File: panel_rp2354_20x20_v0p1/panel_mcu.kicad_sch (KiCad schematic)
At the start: 32 parts, among them SW1 SW_Push, SW2 SW_Push, U1 APS6404L-3SQR, U2 RP2354B_80QFN, Y1 ABM8-272-T3

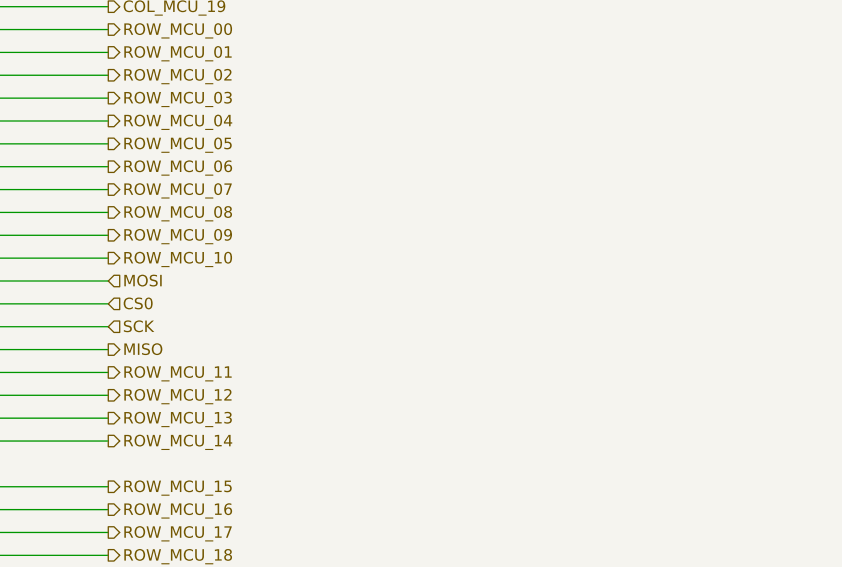
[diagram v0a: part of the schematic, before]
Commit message: Added notes about series termination resistors.
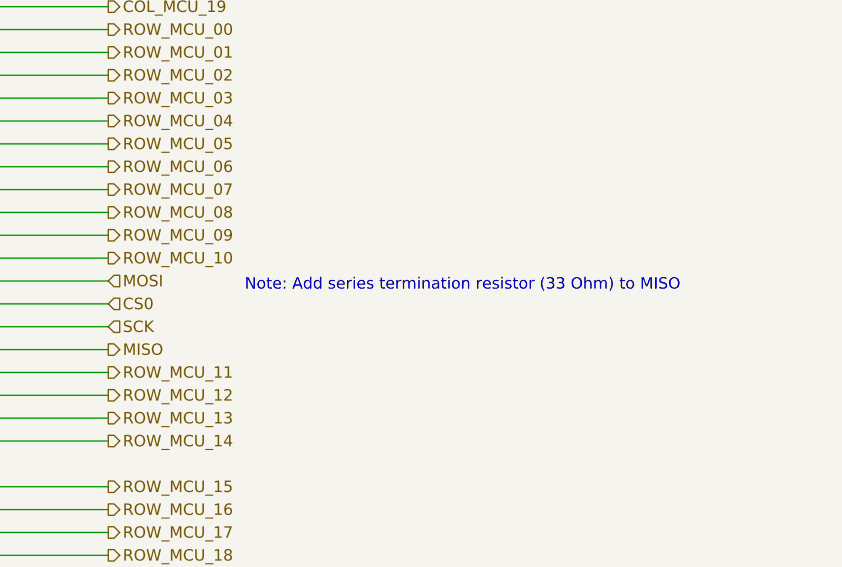
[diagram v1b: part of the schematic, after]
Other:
- note added: "Note: Add series termination resistor (33 Ohm) to MISO"
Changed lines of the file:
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@@
+		)
+	)
+	(text "Note: Add series termination resistor (33 Ohm) to MISO"
+		(exclude_from_sim no)
+		(at 295.91 164.338 0)
+		(effects
+			(font
+				(size 1.27 1.27)
+			)
 		)
 	)

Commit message: Fix most warnings
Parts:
- C1, C10, C11, C12, C13, C14, C15, C16, C17, C18, C2, C3, C6, C9: footprint Capacitor_SMD:C_0201_0603Metric -> panel_custom:C_0201_0603Metric
- C4, C5: footprint RP2350_80QFN_minimal:C_0402_1005Metric_small_pads -> panel_custom:C_0402_1005Metric_small_pads
- C7, C8: footprint Capacitor_SMD:C_0402_1005Metric -> panel_custom:C_0402_1005Metric
- L1: footprint RP2350_80QFN_minimal:L_pol_2016 -> panel_custom:L_pol_2016
- R1, R2, R3, R4, R5, R6, R7, R8: footprint Resistor_SMD:R_0201_0603Metric -> panel_custom:R_0201_0603Metric
- U2: footprint RP2350_80QFN_minimal:RP2350-QFN-80-1EP_10x10_P0.4mm_EP3.4x3.4mm_ThermalVias -> panel_custom:RP2350-QFN-80-1EP_10x10_P0.4mm_EP3.4x3.4mm_ThermalVias
- Y1: footprint Crystal:Crystal_SMD_3225-4Pin_3.2x2.5mm -> panel_custom:Crystal_SMD_3225-4Pin_3.2x2.5mm; symbol Device:Crystal_GND24 -> panel_custom:Crystal_GND24
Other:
- company: (none) -> Janelia Research Campus
- title: (none) -> G6 Panel
